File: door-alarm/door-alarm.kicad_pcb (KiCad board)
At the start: 2 copper layers, 34.5 x 90.5 mm, 14 parts, among them SW1 SW_Reed, U1 TLC555xP

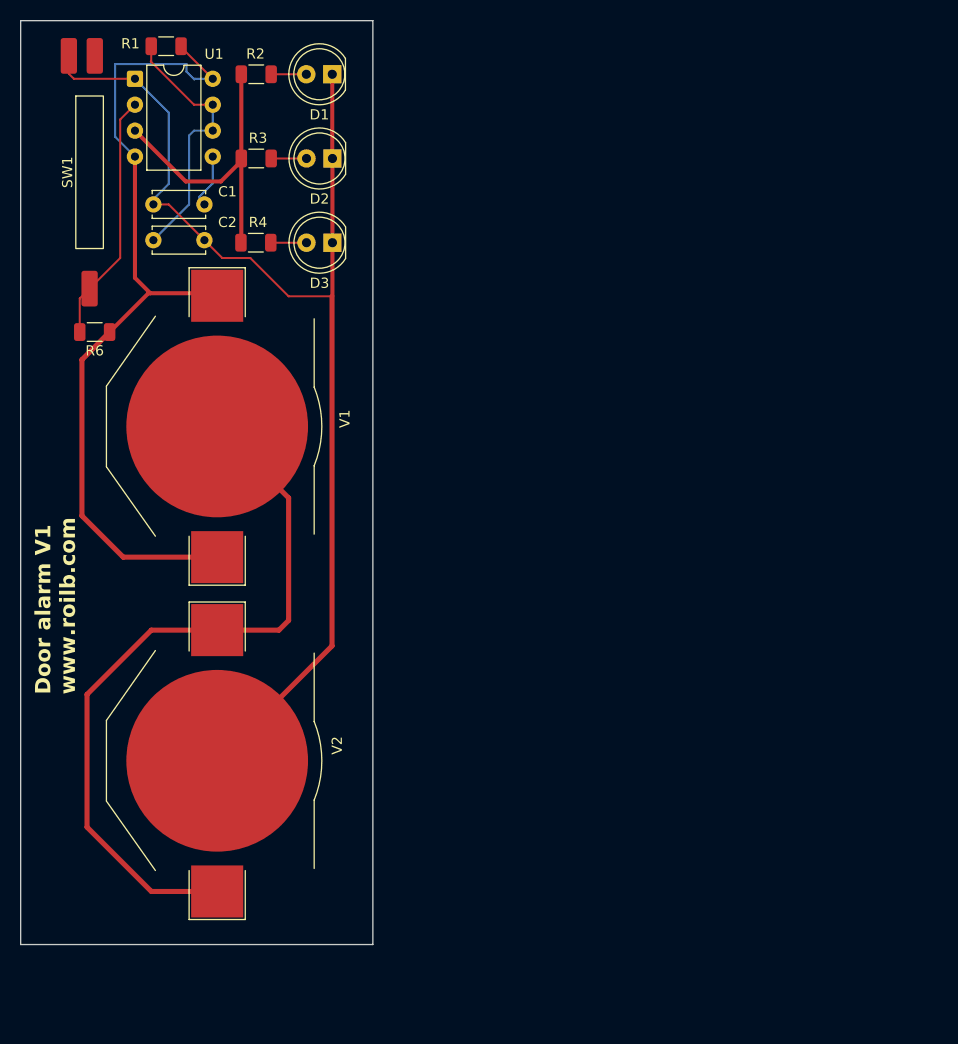
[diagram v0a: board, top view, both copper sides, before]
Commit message: Finished the second version of the alarm, which includes an active buzzer.
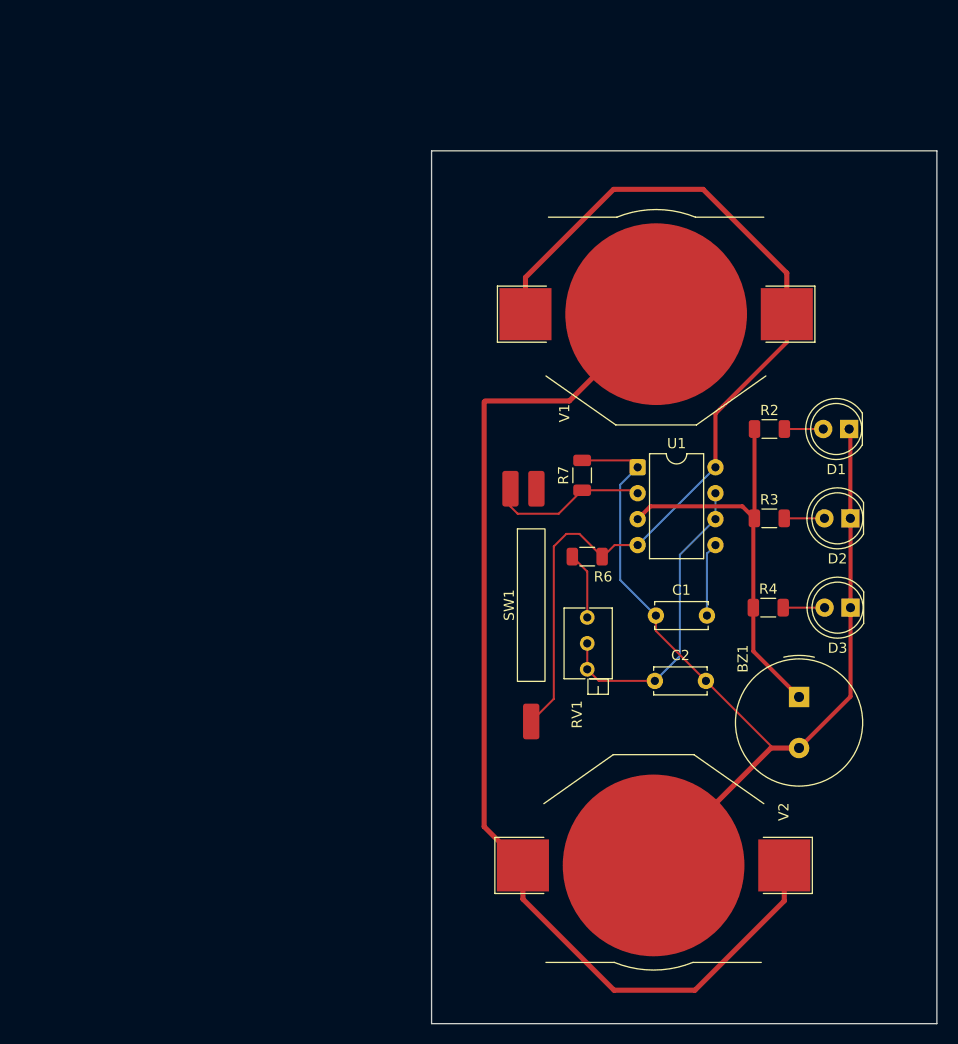
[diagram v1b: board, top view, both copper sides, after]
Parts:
- removed R1: 220 kΩ, Resistor_SMD:R_1206_3216Metric
- added BZ1: Buzzer, Buzzer_Beeper:Buzzer_TDK_PS1240P02BT_D12.2mm_H6.5mm, F.Cu at (154.2, 98.8)
- added R7: 47kΩ, Resistor_SMD:R_1206_3216Metric, F.Cu at (133.0, 77.0)
- added RV1: R_Potentiometer_Trim, Potentiometer_THT:Potentiometer_Bourns_3266Z_Horizontal, F.Cu at (133.5, 91.0)
- R2, R3, R4: value 120Ω -> 180Ω
- R6: value 5.6 kΩ -> 110kΩ
- moved C2 65.4 mm to (140.1, 97.2)
- moved C1 63.6 mm to (140.2, 90.8)
- moved U1 62.2 mm to (138.4, 76.2)
- moved D3 62.1 mm to (159.3, 90.0)
- moved D2 61.8 mm to (159.3, 81.2)
- moved R4 61.6 mm to (151.2, 90.0)
- moved D1 61.4 mm to (159.2, 72.5)
- moved R3 61.4 mm to (151.3, 81.2)
- moved R2 61.1 mm to (151.3, 72.5)
- moved SW1 60.6 mm to (128.0, 89.8)
- moved R6 53.0 mm to (133.5, 85.0)
- moved V1 44.4 mm to (140.2, 61.2), turned to 0 degrees
- moved V2 44.0 mm to (140.0, 115.2), turned to 180 degrees
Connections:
- R6 pad 2: Net-(U1-TRIG) -> Net-(R6-Pad2)
- SW1 pad 1: GND -> Net-(U1-TRIG)
- SW1 pad 2: Net-(U1-TRIG) -> Net-(U1-VCC)
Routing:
- net Net-(V1-Pad2): track 73.0 -> 107.1 mm
- net GND: track 116.2 -> 92.5 mm
- net Net-(BZ1-+): track 29.6 -> 40.6 mm
- net Net-(U1-VCC): track 86.8 -> 97.0 mm
- net Net-(U1-TRIG): track 24.5 -> 15.6 mm
- net Net-(R6-Pad2): track 0.00 -> 6.57 mm
- net Net-(U1-DISCH): track 26.1 -> 30.5 mm
- net Net-(U1-CONT): track 5.23 -> 7.25 mm
- net Net-(D3-A): track 3.50 -> 4.06 mm
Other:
- board size 34.5 x 90.5 mm -> 49.5 x 85.5 mm
- board text removed: "Door alarm V1 www.roilb.com"

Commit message: Added text to both both silkscreens.
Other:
- board text added: "Door alarm v2.0 www.roilb.com"
